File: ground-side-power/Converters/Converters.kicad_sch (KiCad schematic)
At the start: 43 parts, among them J10 Conn_01x03_Female, J11 Ground Connections, J12 Conn_01x04_Female, J13 DAQ Voltage Sensing, J14 DAQ Current Sensing, J27 Conn_01x02_Female, U1 TPS55340, U2 K7805-3AR3, U4 INA180, U5 INA180

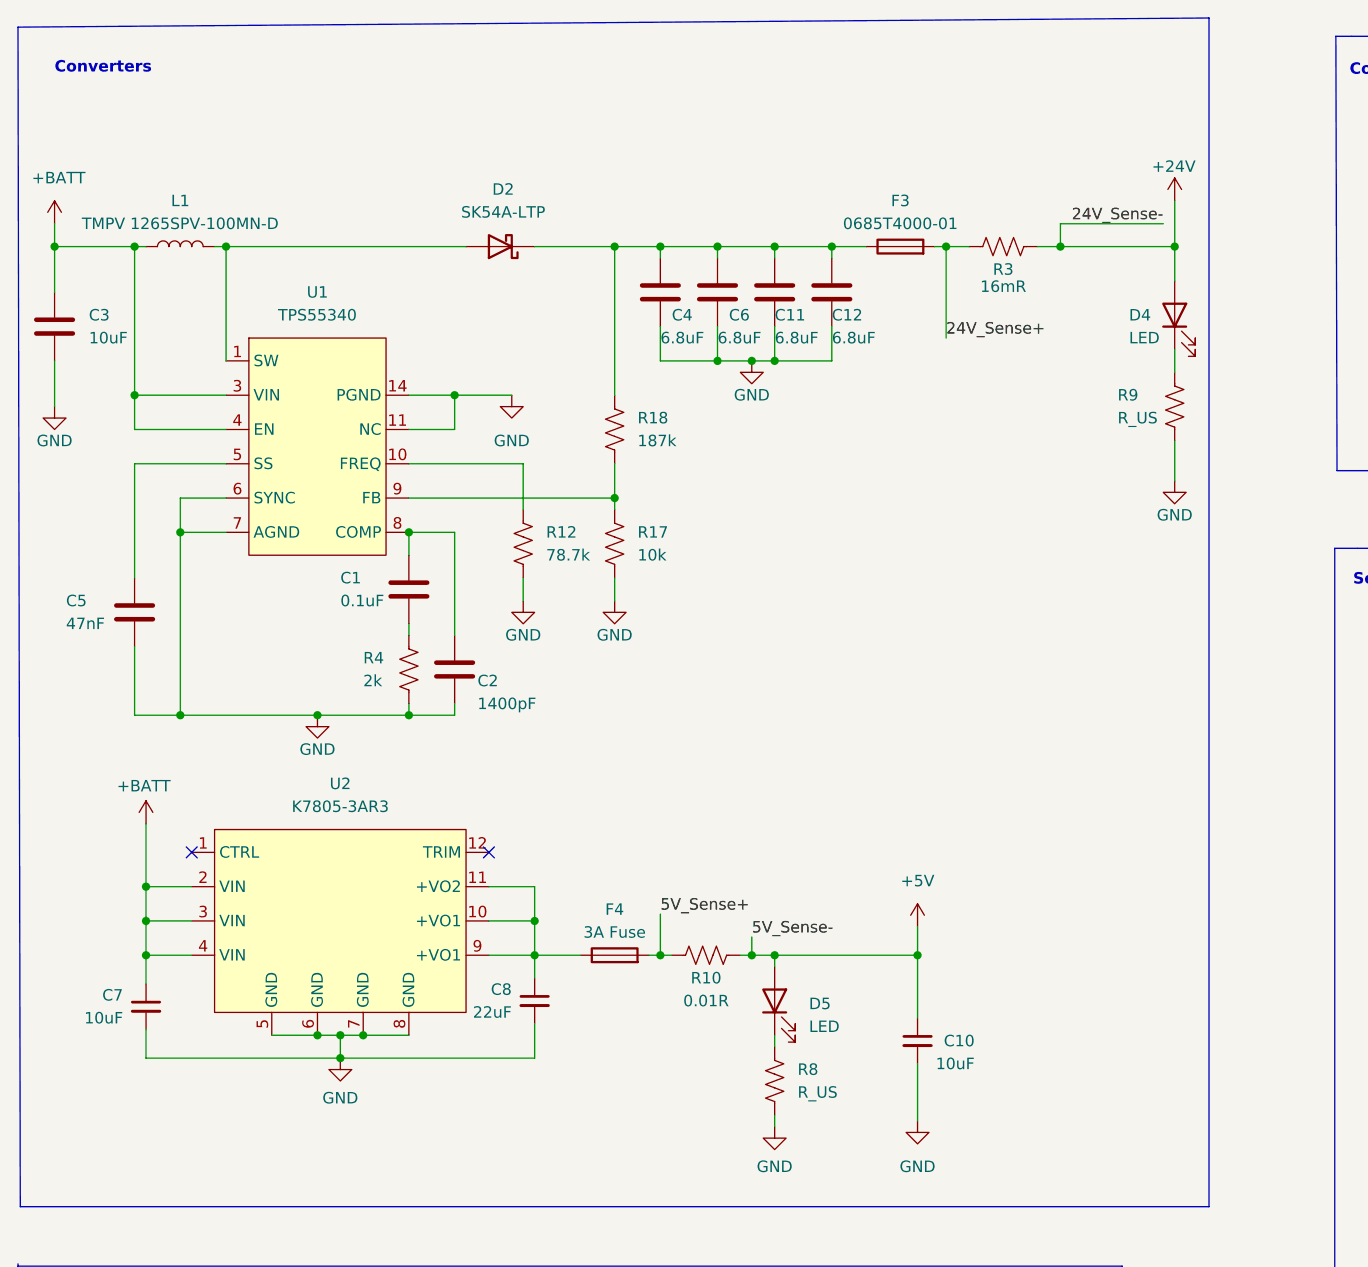
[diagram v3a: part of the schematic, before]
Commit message: added footprints
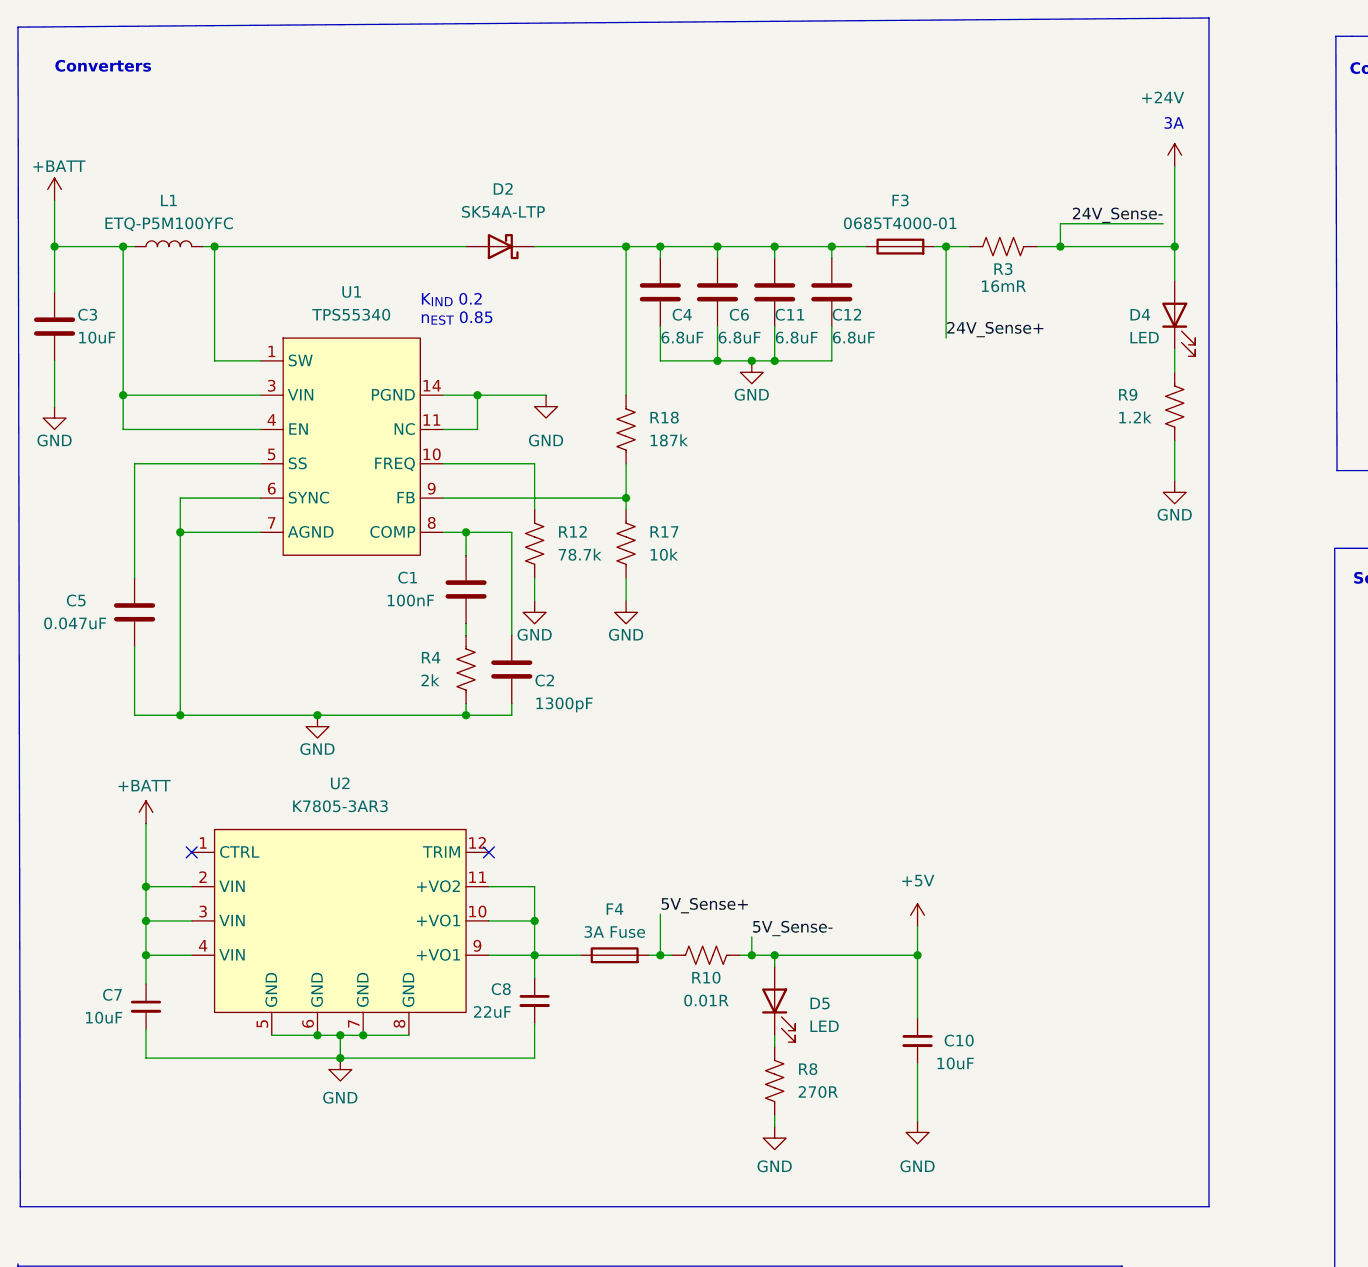
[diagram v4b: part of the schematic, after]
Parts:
- C1: value 0.1uF -> 100nF; footprint Capacitor_SMD:C_0402_1005Metric_Pad0.74x0.62mm_HandSolder -> Diode_SMD:D_0805_2012Metric_Pad1.15x1.40mm_HandSolder
- C11, C12, C3, C4, C6: footprint Capacitor_SMD:C_0805_2012Metric_Pad1.18x1.45mm_HandSolder -> Diode_SMD:D_1206_3216Metric_Pad1.42x1.75mm_HandSolder
- C2: value 1400pF -> 1300pF; footprint Capacitor_SMD:C_0402_1005Metric_Pad0.74x0.62mm_HandSolder -> Diode_SMD:D_0805_2012Metric_Pad1.15x1.40mm_HandSolder
- C5: value 47nF -> 0.047uF; footprint Capacitor_SMD:C_0201_0603Metric_Pad0.64x0.40mm_HandSolder -> Diode_SMD:D_0805_2012Metric_Pad1.15x1.40mm_HandSolder
- D2: footprint (none) -> Diode_SMD:D_SMA_Handsoldering
- D4, D5: footprint (none) -> LED_SMD:LED_1206_3216Metric_Pad1.42x1.75mm_HandSolder
- F3, F4: footprint (none) -> Fuse:Fuseholder_Clip-6.3x32mm_Littelfuse_102_122_Inline_P34.21x7.62mm_D1.98mm_Horizontal
- L1: value TMPV 1265SPV-100MN-D -> ETQ-P5M100YFC; footprint Inductor_SMD:L_Coilcraft_XAL6060-XXX -> Inductor_SMD:L_0805_2012Metric_Pad1.15x1.40mm_HandSolder
- R1: footprint (none) -> Resistor_SMD:R_1206_3216Metric_Pad1.30x1.75mm_HandSolder
- R10: footprint (none) -> Resistor_SMD:R_2512_6332Metric_Pad1.40x3.35mm_HandSolder
- R12, R17, R18, R19, R2, R20, R3, R4, R5, R6: footprint (none) -> Resistor_SMD:R_0805_2012Metric_Pad1.20x1.40mm_HandSolder
- R8: value R_US -> 270R; footprint (none) -> Resistor_SMD:R_0805_2012Metric_Pad1.20x1.40mm_HandSolder
- R9: value R_US -> 1.2k; footprint (none) -> Resistor_SMD:R_0805_2012Metric_Pad1.20x1.40mm_HandSolder
- U1: footprint (none) -> Package_SO:HTSSOP-14-1EP_4.4x5mm_P0.65mm_EP3.4x5mm_Mask3x3.1mm
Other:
- note added: "3A"
- note added: "K_{IND} 0.2 n_{EST} 0.85"
- moved on the sheet: C1, C2, L1, R12, R17, R18, R4, U1

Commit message: Created layout
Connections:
- net +BATT: no longer J10.2 (Pin_2)
- net GND: no longer J10.1 (Pin_1)
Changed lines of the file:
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@@
     )
   )
-  (symbol (lib_id "Connector:Conn_01x02_Female") (at 185.166 32.004 0) (unit 1)
+  (symbol (lib_id "Connector:Conn_01x02_Female") (at 185.42 31.75 0) (unit 1)
     (in_bom yes) (on_board yes) (dnp no) (fields_autoplaced)
-    (property "Reference" "J10" (at 186.436 30.7339 0)
+    (property "Reference" "J10" (at 186.69 30.4799 0)
       (effects (font (size 1.27 1.27)) (justify left))
     )
-    (property "Value" "Conn_01x03_Female" (at 186.436 33.2739 0)
+    (property "Value" "Conn_01x03_Female" (at 186.69 33.0199 0)
       (effects (font (size 1.27 1.27)) (justify left))
     )
-    (property "Footprint" "GSP:1935310" (at 185.166 32.004 0)
+    (property "Footprint" "GSP:1935310" (at 185.42 31.75 0)
       (effects (font (size 1.27 1.27)) hide)
     )
-    (property "Datasheet" "~" (at 185.166 32.004 0)
+    (property "Datasheet" "~" (at 185.42 31.75 0)
       (effects (font (size 1.27 1.27)) hide)
     )

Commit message: implemented comments
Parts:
- added TP1, TP2, TP3: TestPoint, TestPoint:TestPoint_Plated_Hole_D2.0mm, symbol Connector:TestPoint
- F2: renamed from F3; value 0685T4000-01 -> 4A 0685T4000-01
- renumbered C3 to C1, C12 to C10, C10 to C11, C9 to C12, C5 to C2, C7 to C3, C1 to C4, C2 to C5, C8 to C6, C4 to C7, C6 to C8, C11 to C9, D2 to D1, D5 to D2, D4 to D3, F4 to F1, J13 to J1, J14 to J2, J11 to J3, J27 to J4, J12 to J5, J10 to J6, R4 to R1, R2 to R10, R5 to R11, R6 to R12, R19 to R13, R20 to R14, R12 to R2, R18 to R3, R17 to R4, R10 to R5, R8 to R6, R3 to R7, R9 to R8, R1 to R9, U2 to U1, U1 to U2, U4 to U3, U5 to U4
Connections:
- net +24V: now also TP1.1
- net +5V: now also TP2.1
- net +BATT: now also J6.2 (Pin_2), TP3.1
- net GND: now also J6.1 (Pin_1)
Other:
- moved on the sheet: C11

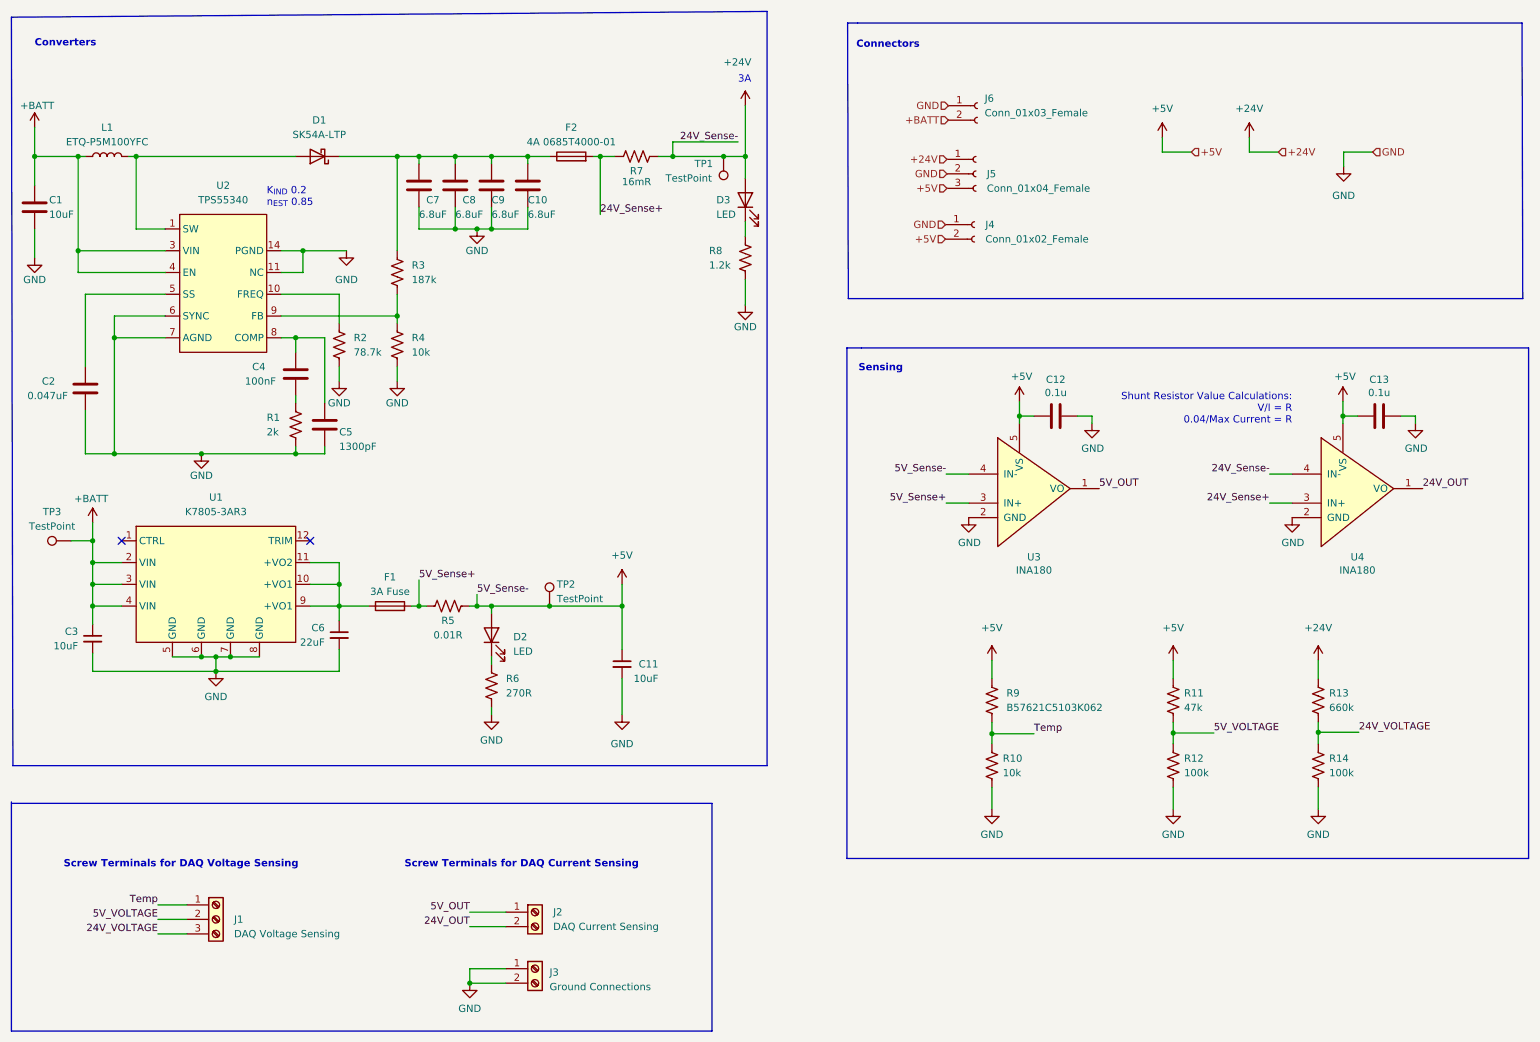
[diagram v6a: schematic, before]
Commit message: sourced vertical screw terminals
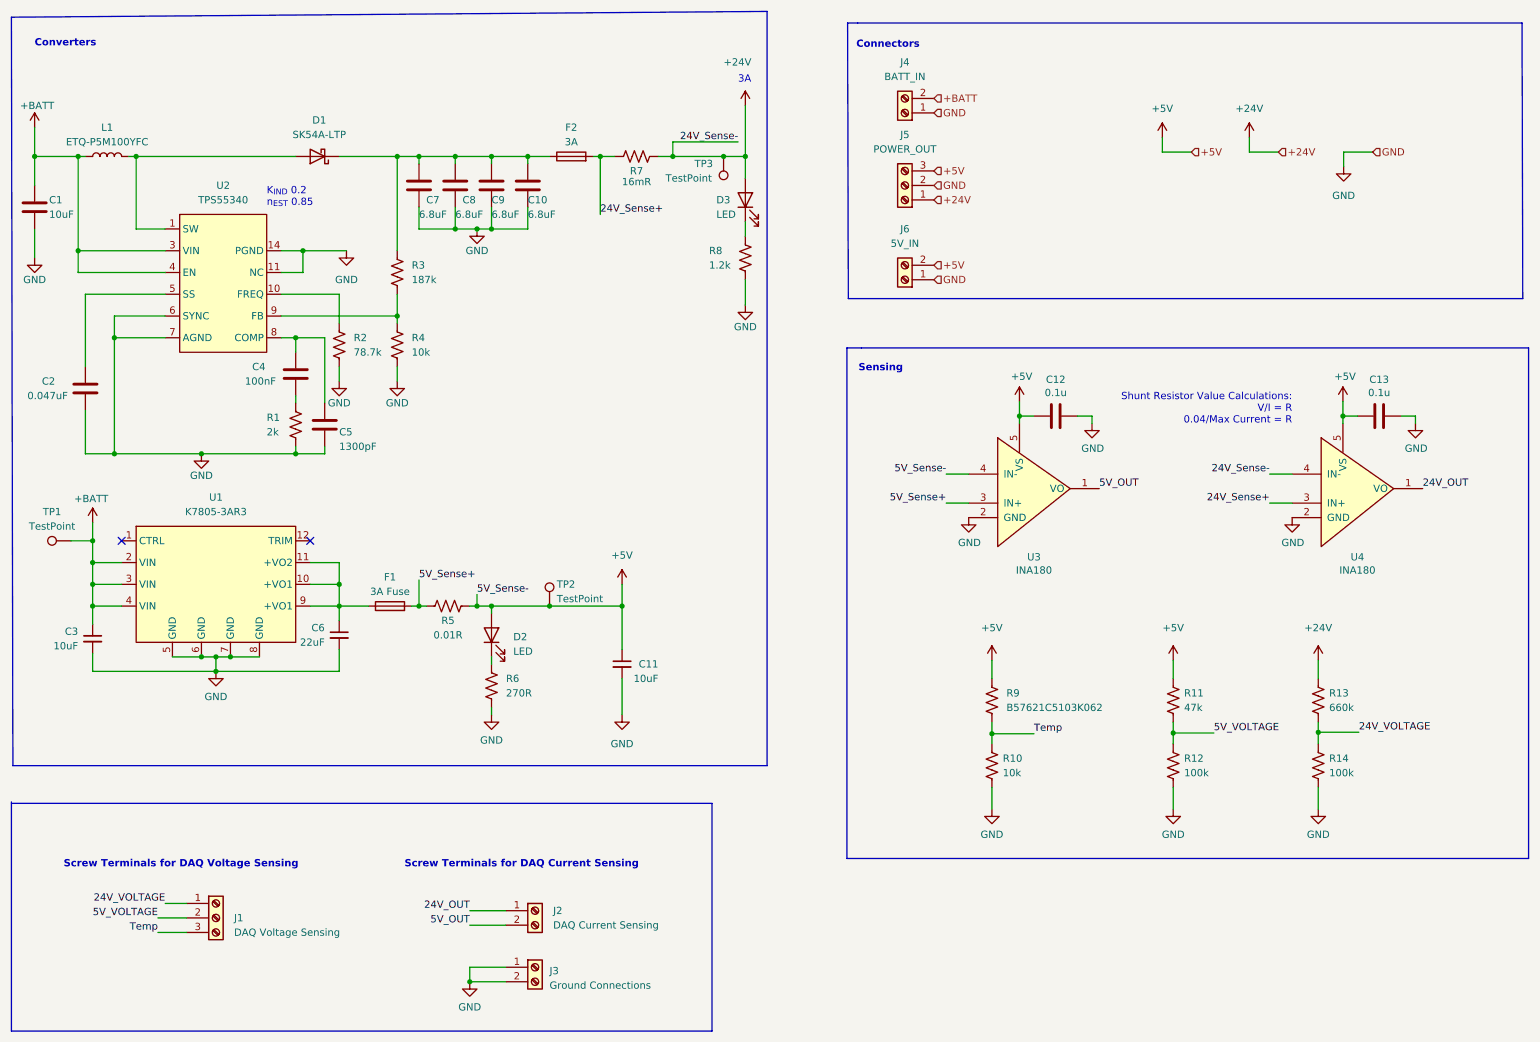
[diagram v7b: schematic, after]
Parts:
- removed J4: Conn_01x02_Female, GSP:1935310, symbol Connector:Conn_01x02_Female
- removed J5: Conn_01x04_Female, GSP:1935323, symbol Connector:Conn_01x03_Female
- removed J6: Conn_01x03_Female, GSP:1935310, symbol Connector:Conn_01x02_Female
- added J4: BATT_IN, TerminalBlock_Phoenix:TerminalBlock_Phoenix_PT-1,5-2-5.0-H_1x02_P5.00mm_Horizontal, symbol Connector:Screw_Terminal_01x02
- added J5: POWER_OUT, TerminalBlock_Phoenix:TerminalBlock_Phoenix_PT-1,5-3-5.0-H_1x03_P5.00mm_Horizontal, symbol Connector:Screw_Terminal_01x03
- added J6: 5V_IN, TerminalBlock_Phoenix:TerminalBlock_Phoenix_PT-1,5-2-5.0-H_1x02_P5.00mm_Horizontal, symbol Connector:Screw_Terminal_01x02
- F2: value 4A 0685T4000-01 -> 3A
- J1: footprint GSP:1935323 -> TerminalBlock_Phoenix:TerminalBlock_Phoenix_PT-1,5-3-5.0-H_1x03_P5.00mm_Horizontal
- J2, J3: footprint GSP:1935310 -> TerminalBlock_Phoenix:TerminalBlock_Phoenix_PT-1,5-2-5.0-H_1x02_P5.00mm_Horizontal
- R5: footprint Resistor_SMD:R_2512_6332Metric_Pad1.40x3.35mm_HandSolder -> Resistor_SMD:R_0805_2012Metric_Pad1.20x1.40mm_HandSolder
- renumbered TP3 to TP1, TP1 to TP3
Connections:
- net +24V: now also J5.1 (Pin_1)
- net +5V: now also J5.3 (Pin_3), J6.2 (Pin_2)
- net +BATT: now also J4.2 (Pin_2)
- net 24V_OUT: now also J2.1 (Pin_1); no longer J2.2 (Pin_2)
- net 24V_VOLTAGE: now also J1.1 (Pin_1); no longer J1.3 (Pin_3)
- net 5V_OUT: now also J2.2 (Pin_2); no longer J2.1 (Pin_1)
- net GND: now also J4.1 (Pin_1), J5.2 (Pin_2), J6.1 (Pin_1)
- net Temp: now also J1.3 (Pin_3); no longer J1.1 (Pin_1)
